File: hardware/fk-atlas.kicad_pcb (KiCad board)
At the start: 2 copper layers, 88.4 x 80.3 mm, 127 parts, among them J1 CONN-HDR-2x5, J2 MICRO-USB, J201 CONN_01X02, J3 Conn_01x02, J301 CONN_01X02, J4 Conn_01x09, J401 CONN_01X02, J501 CONN_01X02, J601 CONN_01X02, P2 ATLAS_EC_PROBE, P3 ATLAS_RTD_PROBE, P4 ATLAS_PH_PROBE, P5 ATLAS_DO_PROBE, P6 ATLAS_ORP_PROBE, Q1 2N7002LT1G, Q2 2N7002LT1G, Q3 2N7002LT1G, Q4 2N7002LT1G, Q5 2N7002LT1G, SW1 SPNO, U1 S25FL1xxK0XM, U2 ATSAMD21G18A-AU, U201 ADM3260, U202 ATLAS_EC, U3 MCP1700T-3302E/MB, U301 ADM3260, U302 ATLAS_RTD, U401 ADM3260, U402 ATLAS_PH, U501 ADM3260, U502 ATLAS_DO, U601 ADM3260, U602 ATLAS_ORP, Y1 FC-135

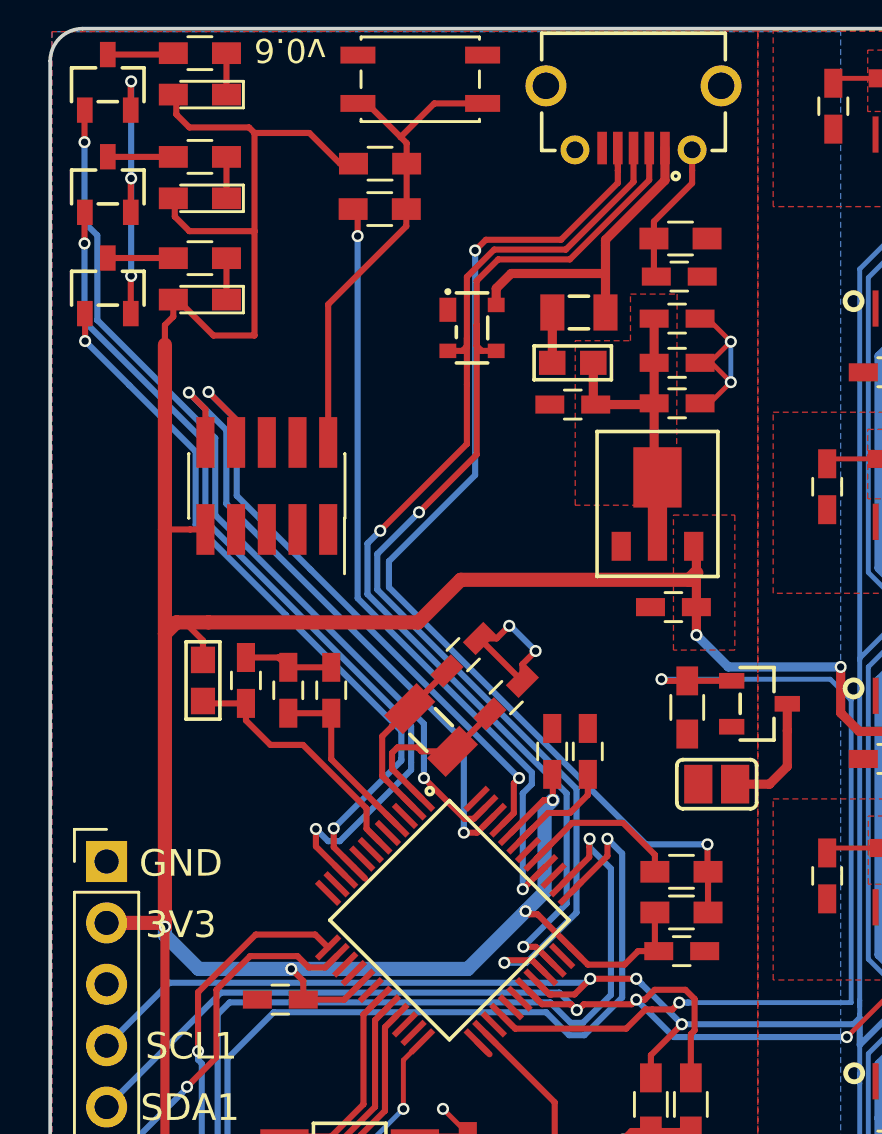
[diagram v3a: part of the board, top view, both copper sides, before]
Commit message: Adding a Vin so we can provide an unregulated voltage.
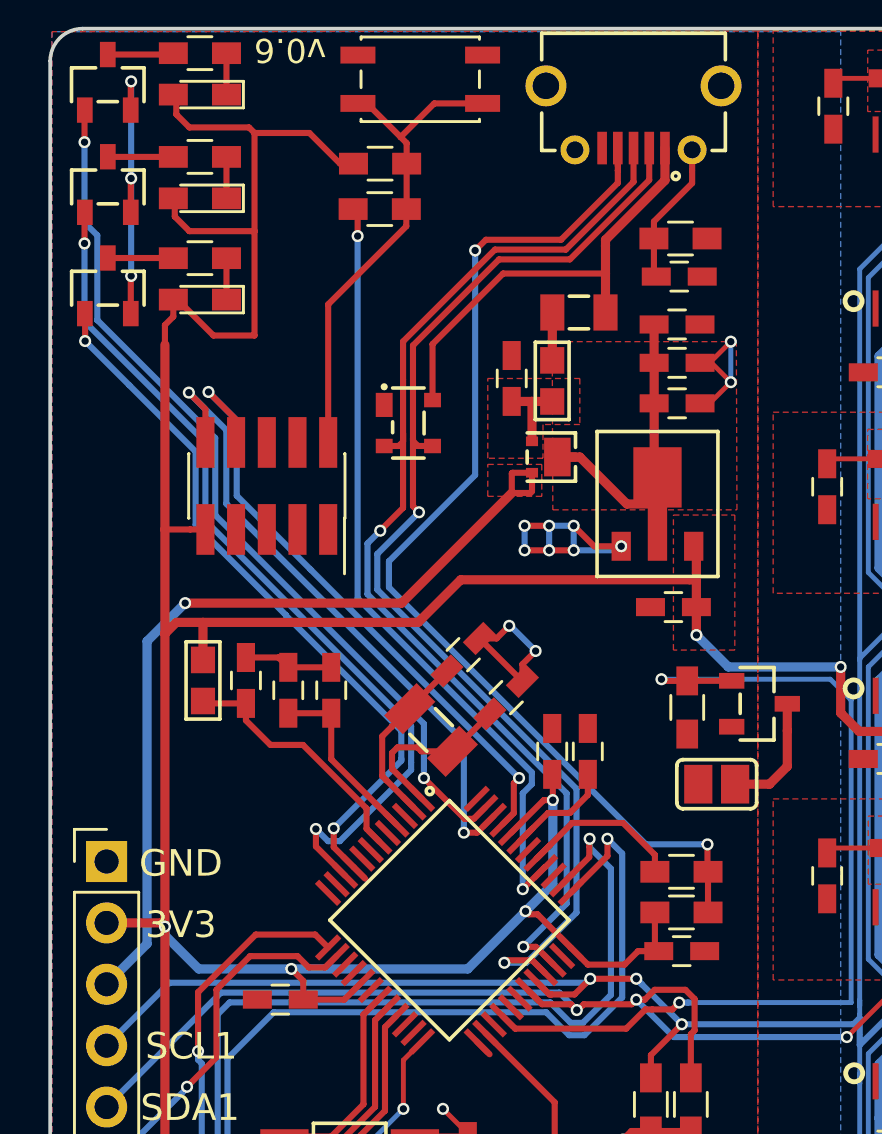
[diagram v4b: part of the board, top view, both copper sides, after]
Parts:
- added D6: DIODE_DUAL_Schottky, RocketScreamKicadLibrary:SOT-1016, F.Cu at (136.5, 75.1)
- moved C10 7.28 mm to (134.8, 71.9), turned to 90 degrees
- moved C11 5.44 mm to (141.7, 69.6), turned to 180 degrees
- moved D5 4.74 mm to (130.6, 73.7)
- moved L2 1.13 mm to (136.5, 72.0), turned to 90 degrees
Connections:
- C11 pad 2: 5V0 -> VBUS
- C12 pad 1: 5V0 -> VBUS
- C14 pad 1: 5V0 -> VBUS
- J4 pad 3: Net-(J4-Pad3) -> VIN
- U3 pad 2: 5V0 -> VBUS
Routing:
- net VIN: track 0.00 -> 35.8 mm, vias 0 -> 1
- net VBUS: track 0.00 -> 13.6 mm
- net GND: track 34.9 -> 44.7 mm, vias 8 -> 15
- net 5V0: track 13.0 -> 3.33 mm
- net VUSB: track 13.3 -> 18.5 mm
- net +3V3: track 336.5 -> 335.5 mm
- net /USB-: track 49.0 -> 48.4 mm
- added copper zone on F.Cu, net VBUS
- added copper zone on F.Cu, net VIN

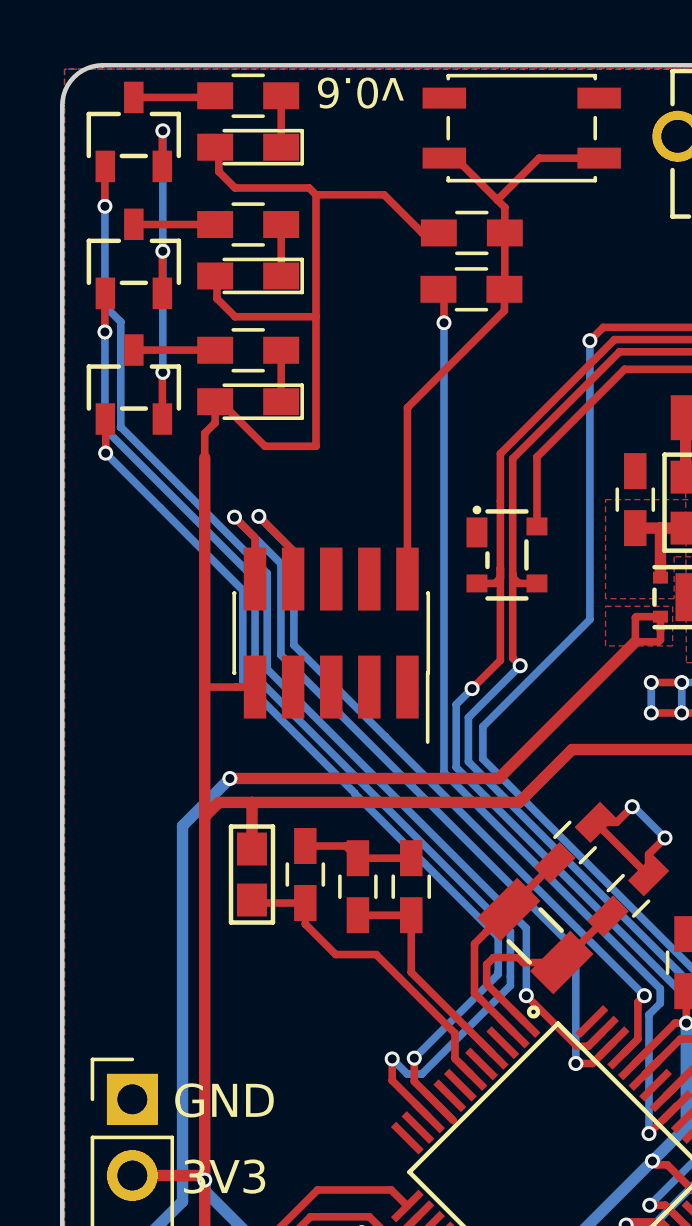
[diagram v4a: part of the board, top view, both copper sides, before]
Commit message: Add labels for LEDs
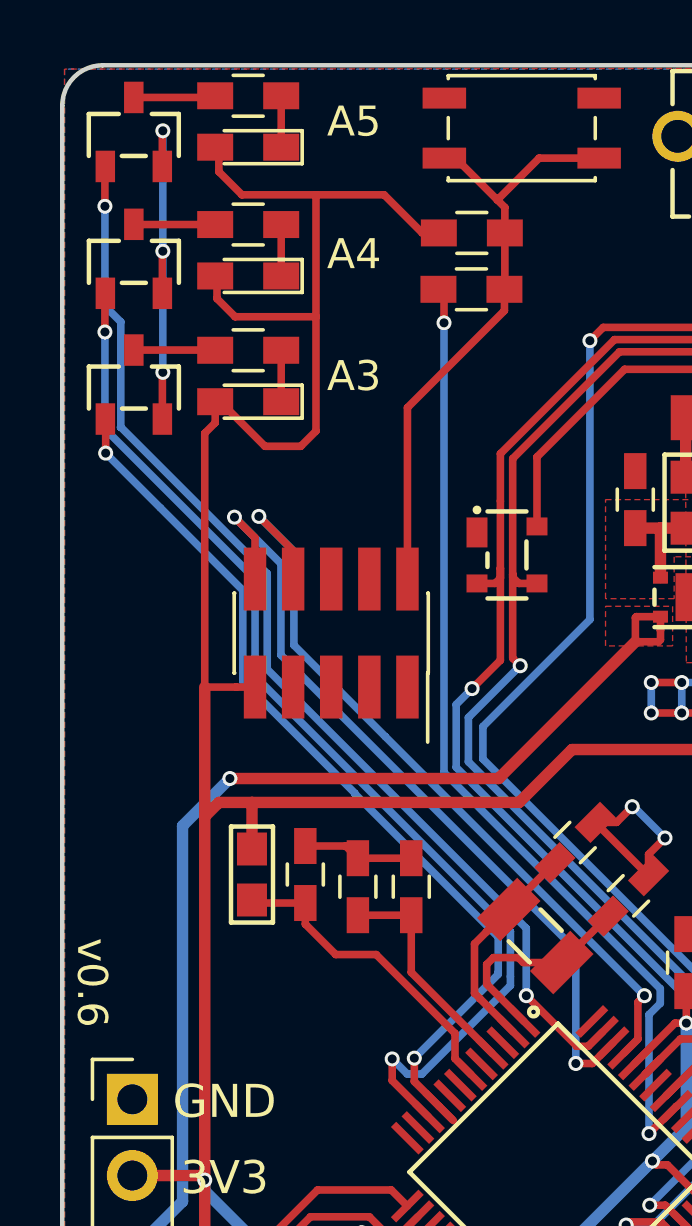
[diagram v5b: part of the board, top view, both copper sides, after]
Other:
- board text added: "A3"
- board text added: "A4"
- board text added: "A5"
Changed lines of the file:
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@@
     (area 115.672799 57.328999 204.214801 137.743001)
     (thickness 1.6)
-    (drawings 27)
-    (tracks 1230)
+    (drawings 30)
+    (tracks 1229)
     (zones 0)
     (modules 128)
@@
       (net 115 VBUS) (solder_mask_margin 0.1))
   )
+  (gr_text A5 (at 125.476 59.2836) (layer F.SilkS)
+    (effects (font (size 1 1) (thickness 0.2)))
+  )
+  (gr_text A4 (at 125.476 63.7032) (layer F.SilkS)
+    (effects (font (size 1 1) (thickness 0.2)))
+  )
+  (gr_text A3 (at 125.476 67.7672) (layer F.SilkS)
+    (effects (font (size 1 1) (thickness 0.2)))
+  )
   (gr_text D31 (at 121.1072 112.268) (layer F.SilkS)
     (effects (font (size 1.1 1.1) (thickness 0.2)))
@@
     (effects (font (size 1.5 1.5) (thickness 0.25)))
   )
-  (gr_text v0.6 (at 125.6792 58.293 180) (layer F.SilkS)
+  (gr_text v0.6 (at 116.7384 87.9856 270) (layer F.SilkS)
     (effects (font (size 1 1) (thickness 0.2)))
   )
@@
   (segment (start 119.0829 59.6061) (end 119.1006 59.5884) (width 0.254) (layer F.Cu) (net 1))
   (via (at 119.1006 59.5884) (size 0.5) (drill 0.3) (layers F.Cu B.Cu) (net 1))
+  (segment (start 124.206 61.722) (end 121.7384 61.722) (width 0.254) (layer F.Cu) (net 2))
+  (segment (start 121.7384 61.722) (end 120.9684 60.952) (width 0.254) (layer F.Cu) (net 2))
+  (segment (start 120.9684 60.952) (end 120.9684 60.198) (width 0.254) (layer F.Cu) (net 2))
+  (segment (start 120.9684 68.6181) (end 121.0184 68.6181) (width 0.254) (layer F.Cu) (net 2))
+  (segment (start 121.0184 68.6181) (end 122.5043 70.104) (width 0.254) (layer F.Cu) (net 2))
+  (segment (start 122.5043 70.104) (end 123.698 70.104) (width 0.254) (layer F.Cu) (net 2))
+  (segment (start 123.698 70.104) (end 124.206 69.596) (width 0.254) (layer F.Cu) (net 2))
+  (segment (start 124.206 69.596) (end 124.206 65.786) (width 0.254) (layer F.Cu) (net 2))
+  (segment (start 120.4976 78.1304) (end 120.4976 69.6699) (width 0.254) (layer F.Cu) (net 2))
+  (segment (start 120.4976 69.6699) (end 120.8454 69.3221) (width 0.254) (layer F.Cu) (net 2))
+  (segment (start 120.8454 69.3221) (end 120.8454 68.6181) (width 0.254) (layer F.Cu) (net 2))
   (segment (start 120.970099 81.975901) (end 122.0724 81.975901) (width 0.381) (layer F.Cu) (net 2))
   (segment (start 122.0724 81.975901) (end 130.977699 81.975901) (width 0.381) (layer F.Cu) (net 2))
@@
   (segment (start 142.2121 80.2132) (end 142.4915 80.2132) (width 0.381) (layer F.Cu) (net 2))
   (segment (start 120.4976 78.1304) (end 120.4976 82.4484) (width 0.381) (layer F.Cu) (net 2))
-  (segment (start 120.4976 70.485) (end 120.4976 78.1304) (width 0.381) (layer F.Cu) (net 2))
   (segment (start 124.968 108.966) (end 132.8928 108.966) (width 0.381) (layer F.Cu) (net 2))
   (segment (start 121.7168 108.966) (end 124.968 108.966) (width 0.381) (layer F.Cu) (net 2))
@@
   (segment (start 135.918287 94.0562) (end 137.290958 95.428871) (width 0.254) (layer F.Cu) (net 2))
   (segment (start 142.4915 79.9338) (end 142.4915 78.9367) (width 0.381) (layer F.Cu) (net 2))
-  (segment (start 120.8454 68.6181) (end 120.8454 69.3221) (width 0.254) (layer F.Cu) (net 2))
-  (segment (start 120.8454 69.3221) (end 120.4976 69.6699) (width 0.254) (layer F.Cu) (net 2))
-  (segment (start 120.4976 69.6699) (end 120.4976 70.485) (width 0.254) (layer F.Cu) (net 2))
   (segment (start 122.174 78.1304) (end 121.545 78.1304) (width 0.254) (layer F.Cu) (net 2))
   (segment (start 121.545 78.1304) (end 120.4976 78.1304) (width 0.254) (layer F.Cu) (net 2))
@@
   (segment (start 126.4772 61.722) (end 124.206 61.722) (width 0.254) (layer F.Cu) (net 2))
   (segment (start 124.206 61.722) (end 124.206 65.786) (width 0.254) (layer F.Cu) (net 2))
-  (segment (start 124.206 65.786) (end 124.206 70.104) (width 0.254) (layer F.Cu) (net 2))
   (segment (start 120.9049 64.4271) (end 120.9049 65.1811) (width 0.254) (layer F.Cu) (net 2))
   (segment (start 120.9049 65.1811) (end 121.5098 65.786) (width 0.254) (layer F.Cu) (net 2))
   (segment (start 121.5098 65.786) (end 124.206 65.786) (width 0.254) (layer F.Cu) (net 2))
-  (segment (start 120.9684 60.198) (end 120.9684 60.952) (width 0.254) (layer F.Cu) (net 2))
-  (segment (start 120.9684 60.952) (end 121.5098 61.4934) (width 0.254) (layer F.Cu) (net 2))
-  (segment (start 121.5098 61.4934) (end 123.9774 61.4934) (width 0.254) (layer F.Cu) (net 2))
-  (segment (start 121.0184 68.6181) (end 120.9684 68.6181) (width 0.254) (layer F.Cu) (net 2))
-  (segment (start 123.9774 61.4934) (end 124.206 61.722) (width 0.254) (layer F.Cu) (net 2))
-  (segment (start 124.206 70.104) (end 122.5043 70.104) (width 0.254) (layer F.Cu) (net 2))
-  (segment (start 122.5043 70.104) (end 121.0184 68.6181) (width 0.254) (layer F.Cu) (net 2))
   (segment (start 140.973648 93.98) (end 141.023648 93.98) (width 0.254) (layer F.Cu) (net 2))
   (segment (start 150.8506 86.4616) (end 150.876 86.487) (width 0.381) (layer F.Cu) (net 2))

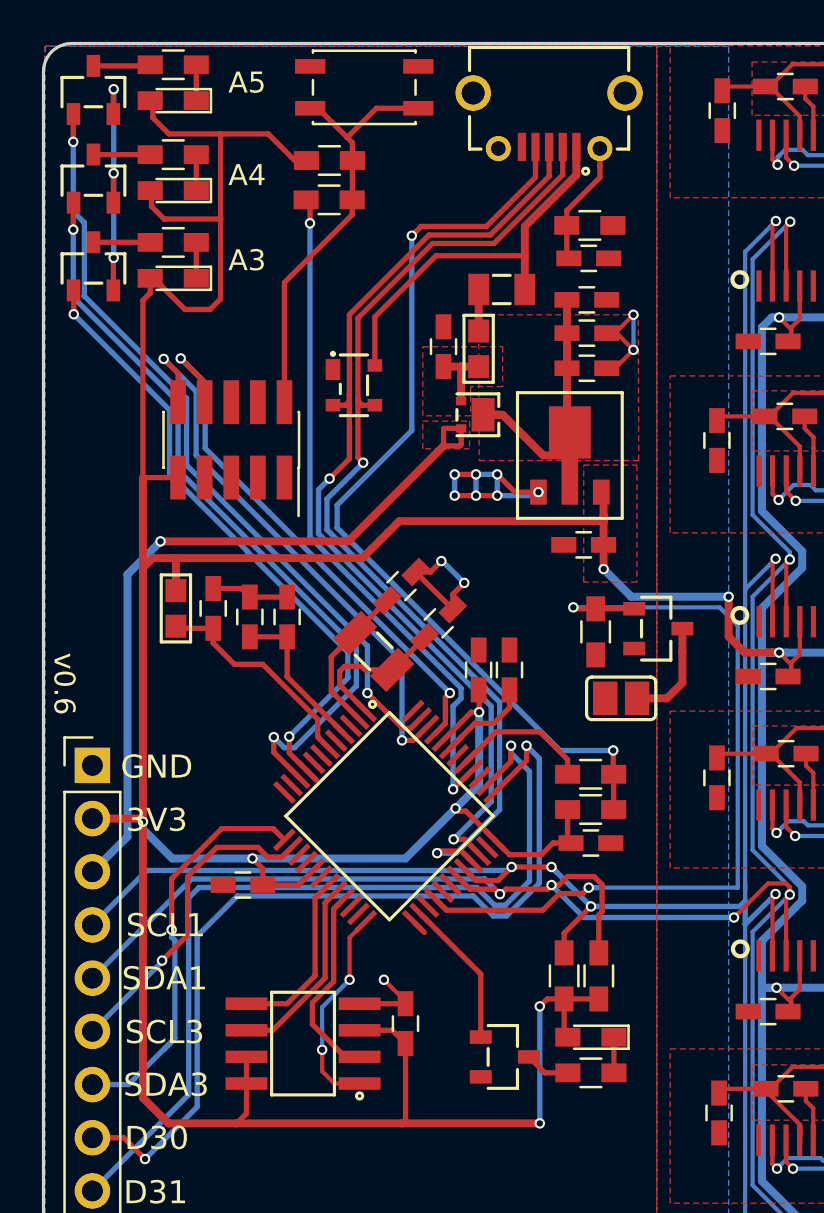
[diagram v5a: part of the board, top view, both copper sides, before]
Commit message: Add LED labels, make room for mounting in one corner.
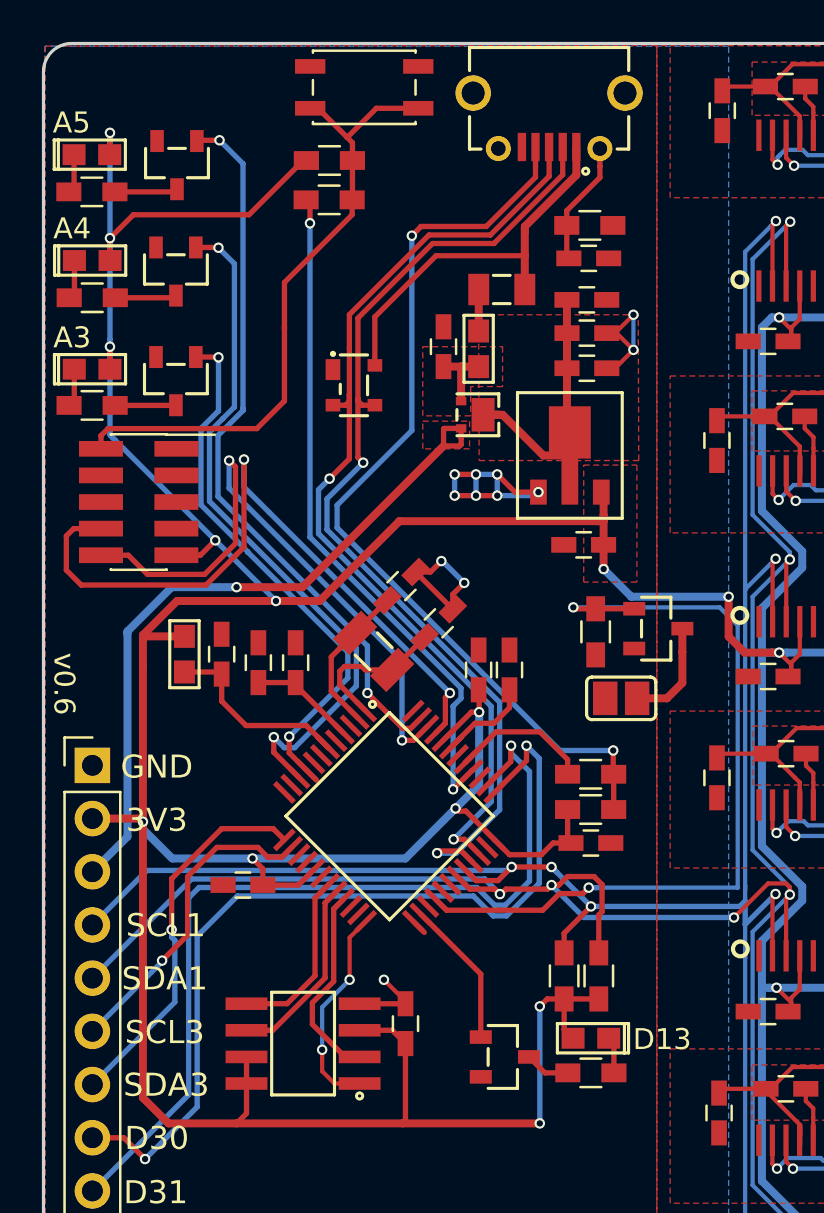
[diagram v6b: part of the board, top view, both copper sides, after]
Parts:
- D1, D2, D3, D4: footprint LEDs:LED_0603_HandSoldering -> RocketScreamKicadLibrary:LED-0603
- moved R3 8.69 mm to (118.1, 74.7), turned to 0 degrees
- moved R6 7.85 mm to (118.1, 69.5), turned to 0 degrees
- moved R7 7.21 mm to (118.1, 64.5), turned to 0 degrees
- moved Q1 6.75 mm to (122.1, 73.5), turned to 180 degrees
- moved Q2 5.93 mm to (122.1, 68.3), turned to 180 degrees
- moved D1 5.82 mm to (118.1, 73.0), turned to 0 degrees
- moved Q3 5.37 mm to (122.1, 63.2), turned to 180 degrees
- moved J1 5.32 mm to (120.3, 79.3), turned to 0 degrees
- moved D2 5.11 mm to (118.1, 67.8), turned to 0 degrees
- moved D3 4.66 mm to (118.1, 62.7), turned to 0 degrees
- moved C1 2.22 mm to (126.0, 87.0)
- moved C2 2.22 mm to (127.8, 87.0)
- moved C7 2.22 mm to (124.3, 86.6)
- moved L1 2.22 mm to (122.5, 86.6)
- moved D4 0.05 mm to (141.9, 104.9)
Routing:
- net GND: track 44.7 -> 28.8 mm, vias 15 -> 12
- net /RST: track 20.4 -> 30.6 mm
- net /SWCLK: track 26.1 -> 34.6 mm
- net /A3: track 30.5 -> 26.2 mm
- net /SWDIO: track 26.8 -> 29.8 mm
- net /A4: track 36.5 -> 33.5 mm
- net AREF: track 7.60 -> 5.15 mm
- net /A5: track 36.9 -> 34.9 mm
- net /SDA3: track 19.7 -> 18.1 mm
- net VIN: track 35.8 -> 34.2 mm
- net +3V3: track 335.2 -> 336.1 mm, vias 17 -> 22
- net Net-(C7-Pad1): track 10.7 -> 9.90 mm
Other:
- board text added: "D13"
